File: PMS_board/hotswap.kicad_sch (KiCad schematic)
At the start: 22 parts, among them Q5 Q_NMOS_GDS, Q6 Q_NMOS_GDS, Q7 Q_NMOS_GDS, Q8 Q_NMOS_GDS, U12 LM74800QDRRRQ1, U9 LM74800QDRRRQ1

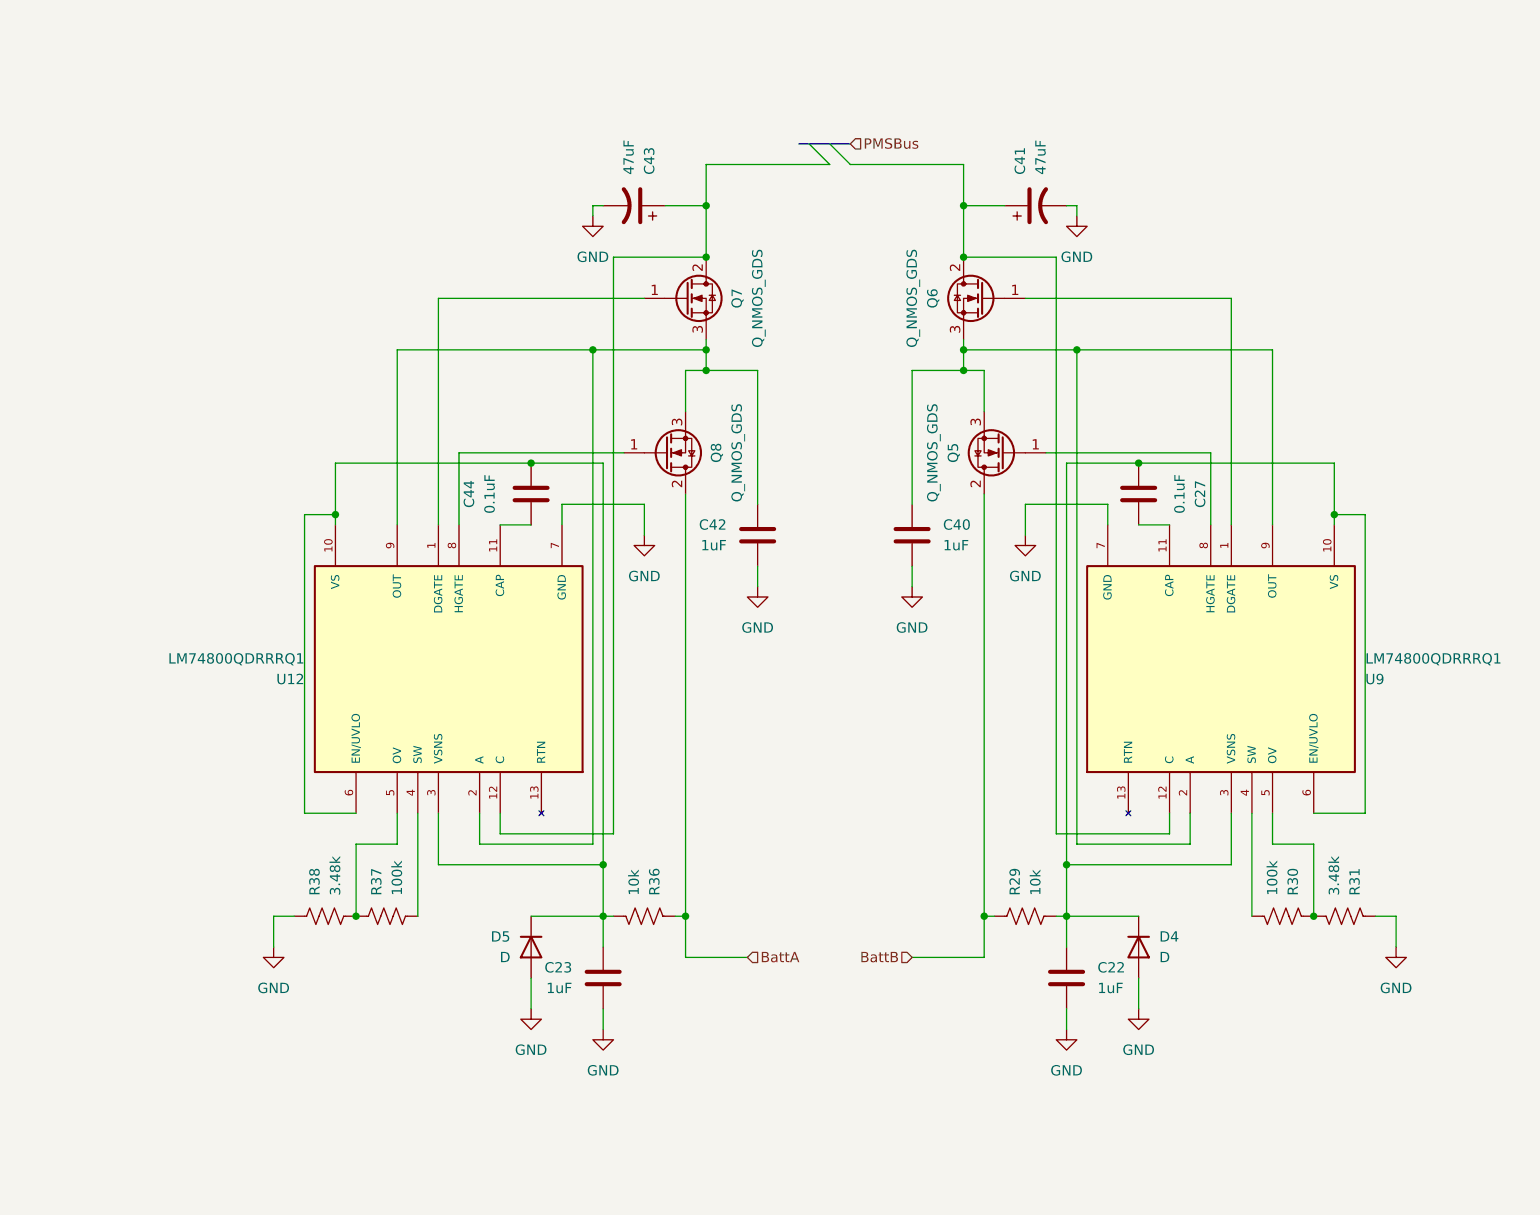
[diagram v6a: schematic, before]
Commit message: add microcontroller pinout
fixed hotswap, added pinouts to microcontroller, and made notes for power smoothing
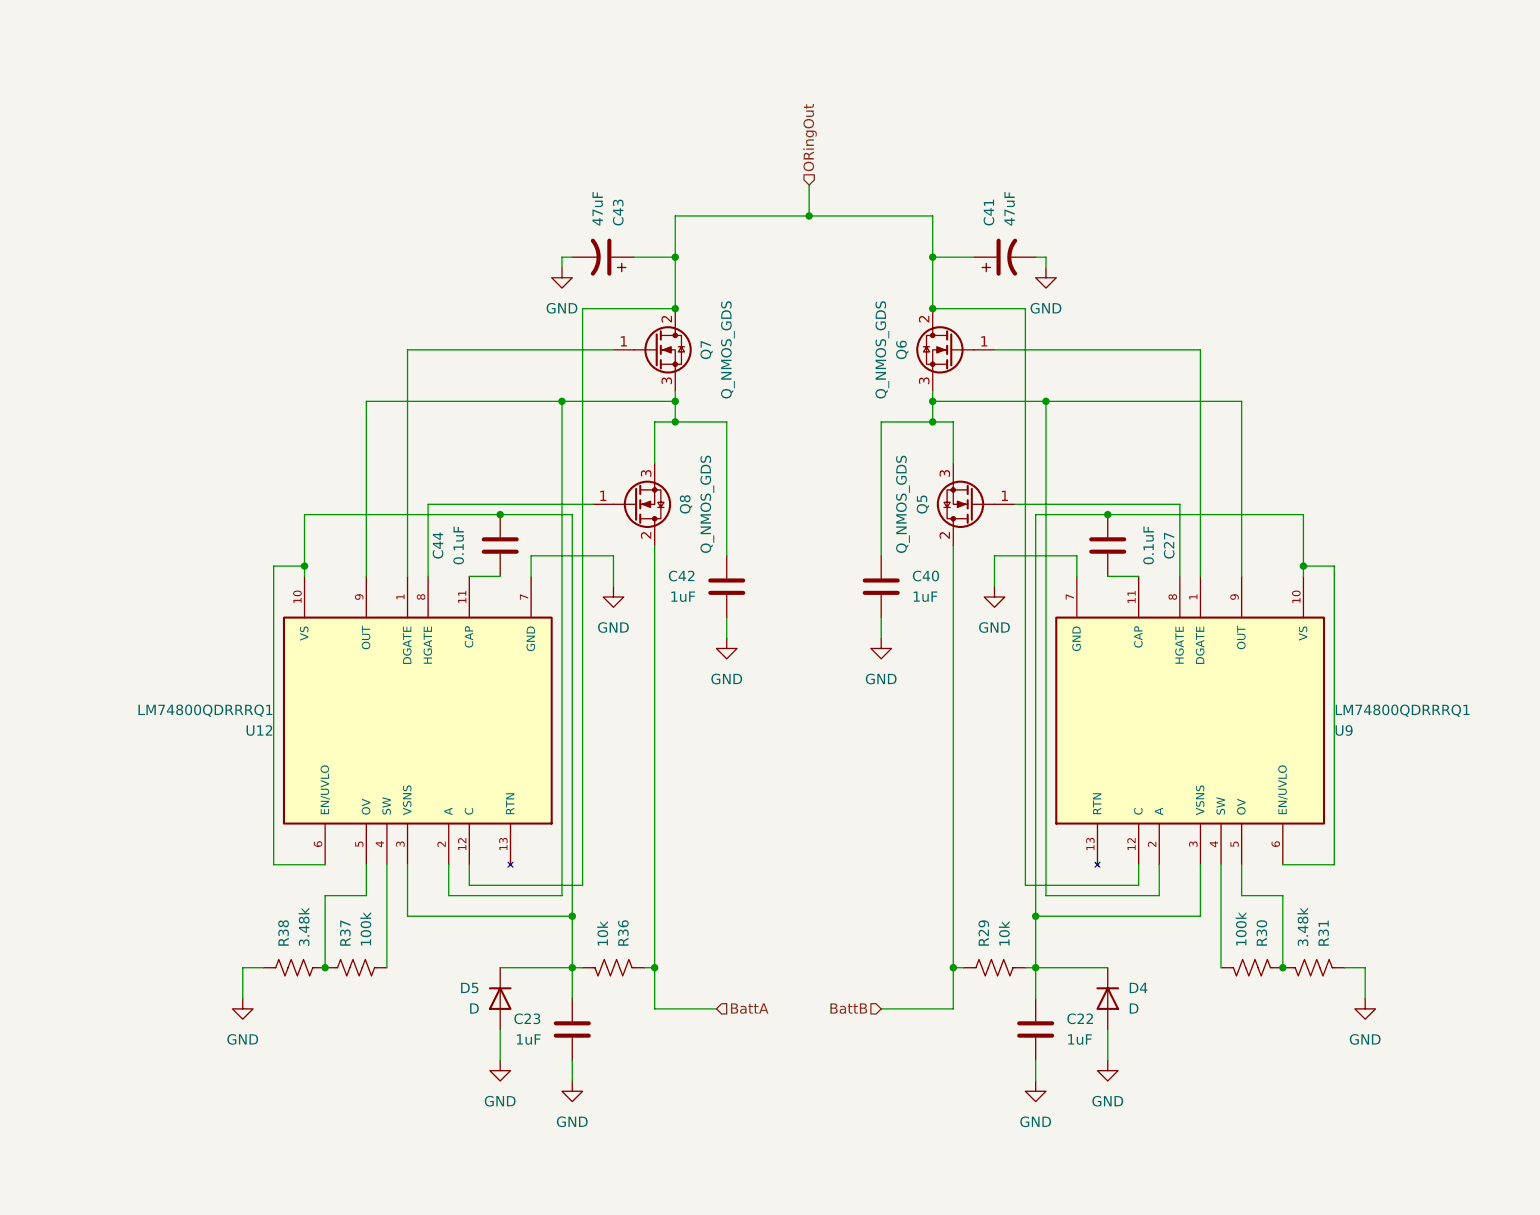
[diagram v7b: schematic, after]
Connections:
- net ORingOut: now reaches C41.1, Q6.2 (D), U9.12 (C)
- net ORingOut: now also C43.1, Q7.2 (D), U12.12 (C)
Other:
- moved on the sheet: C22, C23, C27, C40, C41, C42, C43, C44, D4, D5, Q5, Q6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
